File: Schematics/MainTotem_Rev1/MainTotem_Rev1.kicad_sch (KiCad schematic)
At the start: 0 parts

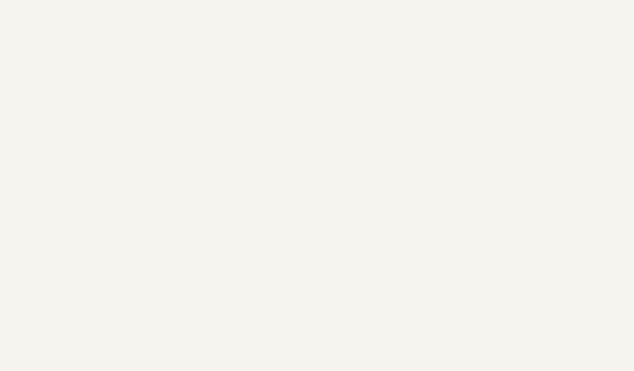
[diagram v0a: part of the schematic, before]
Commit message: Added RS485 functionality to MainTotemLite
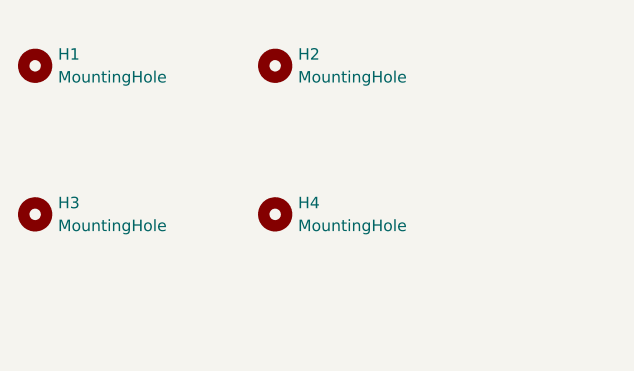
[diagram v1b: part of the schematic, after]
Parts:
- added H1, H2, H3, H4: MountingHole, symbol Mechanical:MountingHole

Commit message: Adding the MTL Schematics in post editing
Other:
- removed sheet LEDsGPIO
- added sheet Clock (clock.kicad_sch)
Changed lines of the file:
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@@
+	)
+	(sheet
+		(at 151.13 111.76)
+		(size 16.51 6.35)
+		(exclude_from_sim no)
+		(in_bom yes)
+		(on_board yes)
+		(dnp no)
+		(fields_autoplaced yes)
+		(stroke
+			(width 0.1524)
+			(type solid)
+		)
+		(fill
+			(color 0 0 0 0.0000)
+		)
+		(property "Sheetname" "Clock"
+			(at 151.13 111.0484 0)
+			(effects
+				(font
+					(size 1.27 1.27)
+				)
+				(justify left bottom)
+			)
+		)
+		(property "Sheetfile" "clock.kicad_sch"
+			(at 151.13 118.6946 0)
+			(effects
+				(font
+					(size 1.27 1.27)
+				)
+				(justify left top)
+			)
+		)
+		(instances
+			(project "MainTotem_Rev1"
+				(path "/f88ba0f4-041f-4cf3-b904-3ea5c6101abb"
+					(page "9")
+				)
+			)
+		)
 	)
 	(sheet
@@
 				)
 			)
-		)
-	)
-	(sheet
-		(at 151.13 72.39)
-		(size 16.51 6.35)
-		(exclude_from_sim no)
-		(in_bom yes)
-		(on_board yes)
-		(dnp no)
-		(fields_autoplaced yes)
-		(stroke
-			(width 0.1524)
-			(type solid)
-		)
-		(fill
-			(color 0 0 0 0.0000)
-		)
-		(property "Sheetname" "LEDsGPIO"
-			(at 151.13 71.6784 0)
-			(effects
-				(font
-					(size 1.27 1.27)
-				)
-				(justify left bottom)
-			)
-		)
-		(property "Sheetfile" "LEDsGPIO.kicad_sch"
-			(at 151.13 79.3246 0)
-			(effects
-				(font
-					(size 1.27 1.27)
-				)
-				(justify left top)
-			)
-		)
-		(instances
-			(project "MainTotem_Rev1"
-				(path "/f88ba0f4-041f-4cf3-b904-3ea5c6101abb"
-					(page "7")
-				)
-			)

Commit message: Layout Edits for Mezzanine Connector routing
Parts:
- H1, H2, H3, H4: footprint (none) -> MountingHole:MountingHole_3.2mm_M3_Pad_TopOnly
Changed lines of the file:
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@@
 			)
 		)
-		(property "Footprint" ""
+		(property "Footprint" "MountingHole:MountingHole_3.2mm_M3_Pad_TopOnly"
 			(at 66.04 74.93 0)
 			(effects
@@
 			)
 		)
-		(property "Footprint" ""
+		(property "Footprint" "MountingHole:MountingHole_3.2mm_M3_Pad_TopOnly"
 			(at 39.37 91.44 0)
 			(effects
@@
 			)
 		)
-		(property "Footprint" ""
+		(property "Footprint" "MountingHole:MountingHole_3.2mm_M3_Pad_TopOnly"
 			(at 66.04 91.44 0)
 			(effects
@@
 			)
 		)
-		(property "Footprint" ""
+		(property "Footprint" "MountingHole:MountingHole_3.2mm_M3_Pad_TopOnly"
 			(at 39.37 74.93 0)
 			(effects
